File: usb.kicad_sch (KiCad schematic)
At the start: 15 parts, among them J1 USB_A, J2 USB_A, J4 USB_C_Receptacle_USB2.0, U1 FE1.1s, U3 SRV05-4, U4 SRV05-4, Y1 12MHz

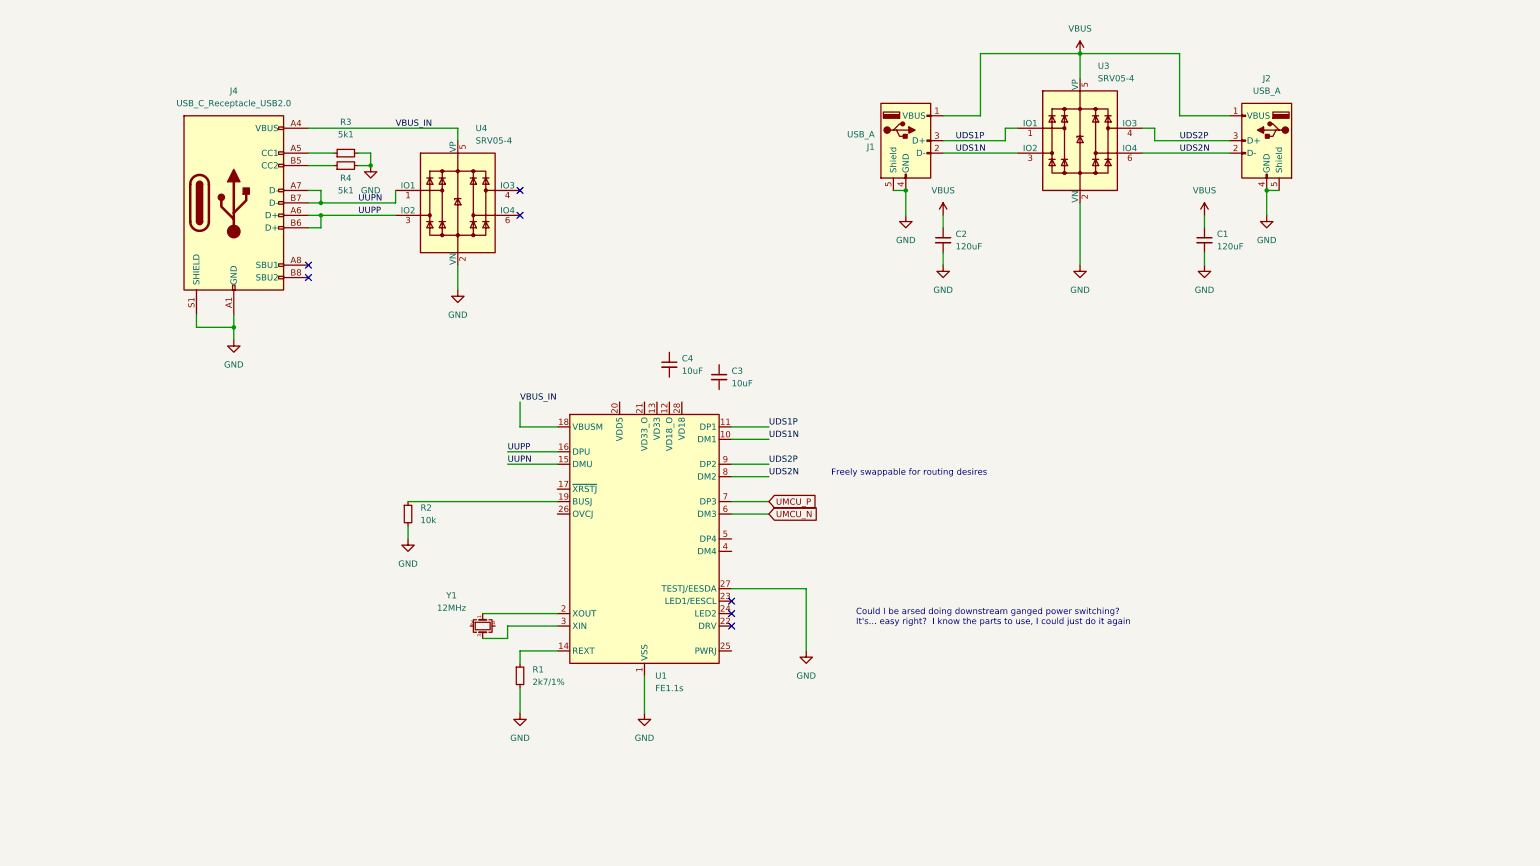
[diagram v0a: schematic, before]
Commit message: sch nearing completion.
usb side done.
needs mcu power supply sorting out.
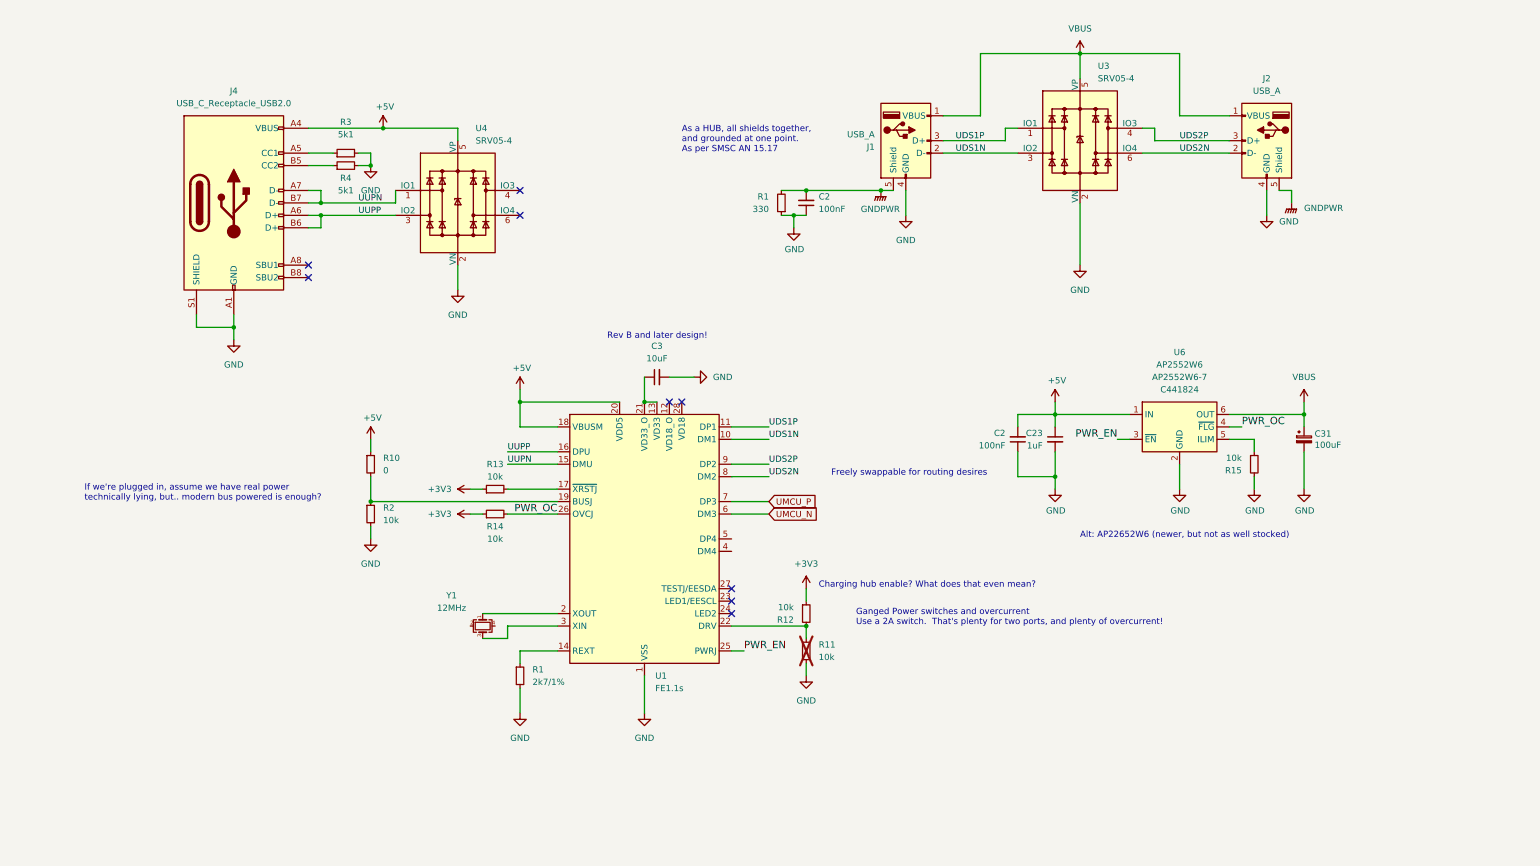
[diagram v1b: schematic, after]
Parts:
- removed C1, C2: 120uF, Capacitor_SMD:C_1206_3216Metric, symbol Device:C_Small
- removed C4: 10uF, Capacitor_SMD:C_0805_2012Metric, symbol Device:C_Small
- added C2 (x2): 100nF, Capacitor_SMD:C_0603_1608Metric, symbol Device:C_Small
- added C23: 1uF, Capacitor_SMD:C_0603_1608Metric, symbol Device:C_Small
- added C31: 100uF, Capacitor_SMD:C_1206_3216Metric, symbol Device:C_Polarized_Small
- added R1: 330, Resistor_SMD:R_0603_1608Metric, symbol Device:R_Small
- added R10: 0, Resistor_SMD:R_0603_1608Metric, symbol Device:R_Small
- added R11, R12, R13, R14, R15: 10k, Resistor_SMD:R_0603_1608Metric, symbol Device:R_Small
- added U6: AP2552W6, Package_TO_SOT_SMD:SOT-23-6, symbol karl-parts:AP2552W6
- C3: MPN (none) -> CL21A106KAYNNNE; jlc-basic (none) -> 1; lcsc# (none) -> C15850
- R1: MPN (none) -> 0603WAF2701T5E; jlc-basic (none) -> 1; lcsc# (none) -> C13167
- R2: MPN (none) -> 0603WAF1002T5E; jlc-basic (none) -> 1; lcsc# (none) -> C25804
- R3, R4: MPN (none) -> 0603WAF5101T5E; jlc-basic (none) -> 1; lcsc# (none) -> C23186
- U1: jlc-basic (none) -> 0
- U3, U4: jlc-basic (none) -> 1; lcsc# C5180248 -> C85364
- Y1: jlc-basic (none) -> 1
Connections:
- net VBUS_IN is gone; now on net +5V: J4.A4 (VBUS), J4.A9 (VBUS), J4.B4 (VBUS), J4.B9 (VBUS), U1.18 (VBUSM), U4.5 (VP)
- net GND: now also C3.2, C2.1, C2.1, C23.2, C31.2, R1.1, R11.1, R15.2, U6.2 (GND); no longer J1.5 (Shield), J2.5 (Shield), U1.27 (TESTJ/EESDA)
- net VBUS: now also C31.1, U6.6 (OUT)
- net at R2.1, U1.19 (BUSJ): now also R10.2
- net at C3.1: now also U1.13 (VD33), U1.21 (VD33_O)
- net at U1.17 (~{XRSTJ}): now also R13.2
- net +5V: now reaches U1.20 (VDD5)
- net +5V: now also C2.2, C23.1, R10.1, U6.1 (IN)
- net at U1.22 (DRV): now also R11.2, R12.2
- net PWR_EN: now reaches U1.25 (PWRJ)
- net PWR_EN: now also U6.3 (~{EN})
- net PWR_OC: now reaches U1.26 (OVCJ)
- net PWR_OC: now also R14.2, U6.4 (~{FLG})
- new net: R15.1, U6.5 (ILIM)
- new net +3V3: R12.1, R13.1, R14.1
- new net GNDPWR: C2.2, J1.5 (Shield), J2.5 (Shield), R1.2
- no-connect marks 7 -> 9
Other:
- note added: "Alt: AP22652W6 (newer, but not as well stocked)"
- note added: "As a HUB, all shields together, and grounded at one point. As per SMSC AN 15.17"
- note added: "Charging hub enable? What does that even mean?"
- note added: "Ganged Power switches and overcurrent Use a 2A switch. That's plenty for two ports, and plenty of overcurrent!"
- note added: "If we're plugged in, assume we have real power technically lying, but.. modern bus powered is enough?"
- note added: "Rev B and later design!"
- note removed: "Could I be arsed doing downstream ganged power switching? It's... easy right? I know the parts to use, I could just do it again"
- moved on the sheet: C3, R2

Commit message: schematic "done" footprints all assigned
Need working calipers to start getting the board outline and fixed
positions, but ... mostly there?

schematic needs "polish" now, more introductions, cleaner text layouts,
probably more optional test points, throw more caps at it.
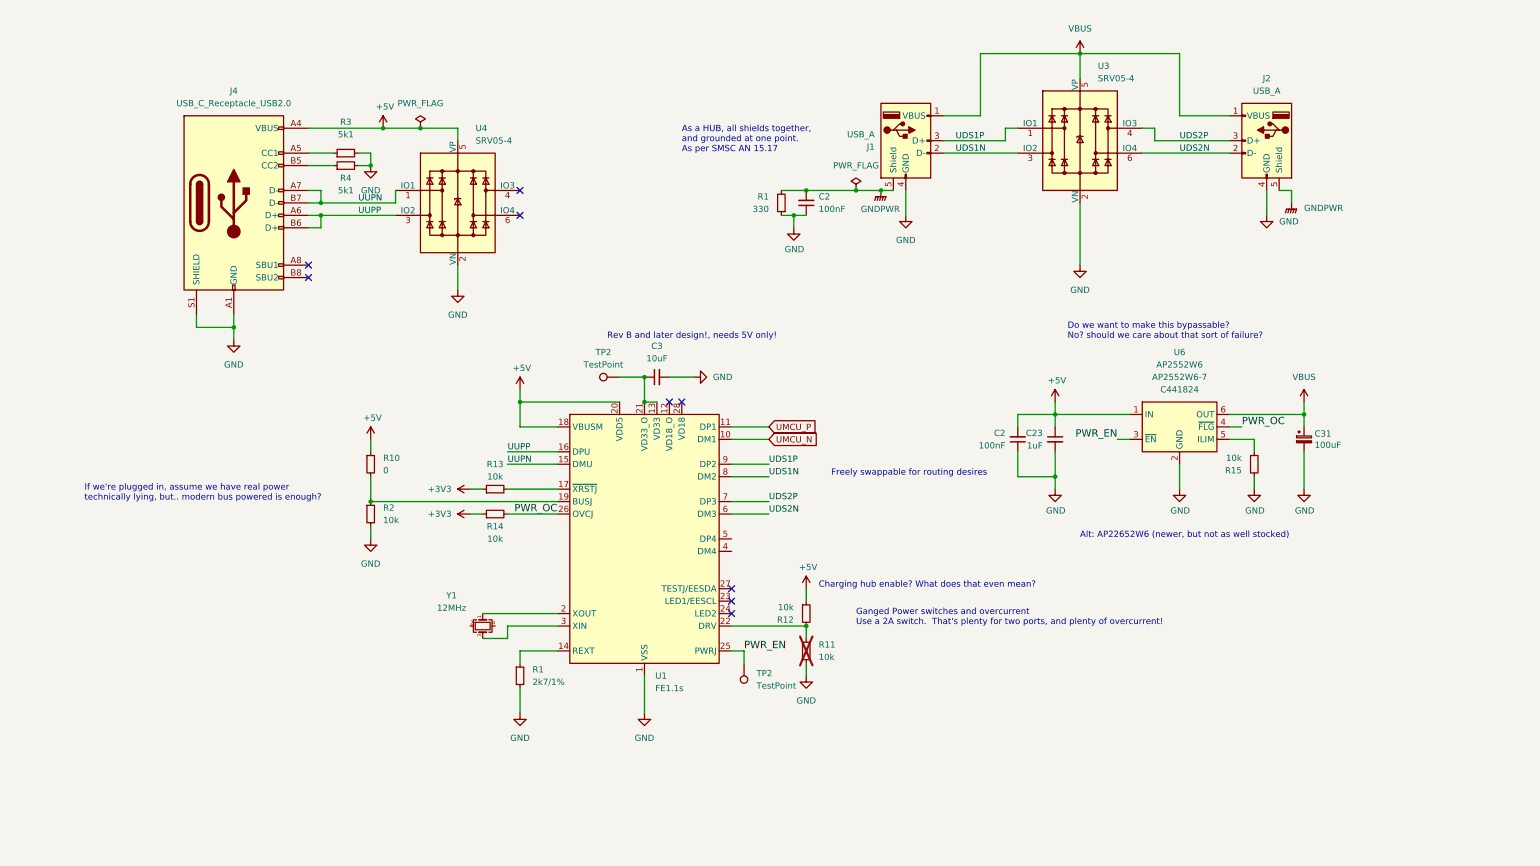
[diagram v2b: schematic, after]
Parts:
- added TP2 (x2): TestPoint, TestPoint:TestPoint_THTPad_D1.5mm_Drill0.7mm, symbol Connector:TestPoint
- J1, J2: footprint (none) -> Connector_USB:USB_A_Stewart_SS-52100-001_Horizontal; MPN (none) -> 902-141A1011D10100; jlc-basic (none) -> 0; lcsc# C42436 -> C42643
- J4: footprint (none) -> Connector_USB:USB_C_Receptacle_G-Switch_GT-USB-7010ASV; MPN (none) -> USB-TYPE-C-018; jlc-basic (none) -> 0; lcsc# C2765186 -> C2927038
- R1, R3, R4: footprint (none) -> Resistor_SMD:R_0603_1608Metric
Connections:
- net +3V3: no longer R12.1
- net +5V: now also R12.1
- net PWR_EN: now also TP2.1
- net UDS1N: now also U1.8 (DM2); no longer U1.10 (DM1)
- net UDS1P: now also U1.9 (DP2); no longer U1.11 (DP1)
- net UDS2N: now also U1.6 (DM3); no longer U1.8 (DM2)
- net UDS2P: now also U1.7 (DP3); no longer U1.9 (DP2)
- net UMCU_N: now also U1.10 (DM1); no longer U1.6 (DM3)
- net UMCU_P: now also U1.11 (DP1); no longer U1.7 (DP3)
- net at C3.1, U1.13 (VD33), U1.21 (VD33_O): now also TP2.1
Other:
- note added: "Do we want to make this bypassable? No? should we care about that sort of failure?"
- note added: "Rev B and later design!, needs 5V only!"
- note removed: "Rev B and later design!"

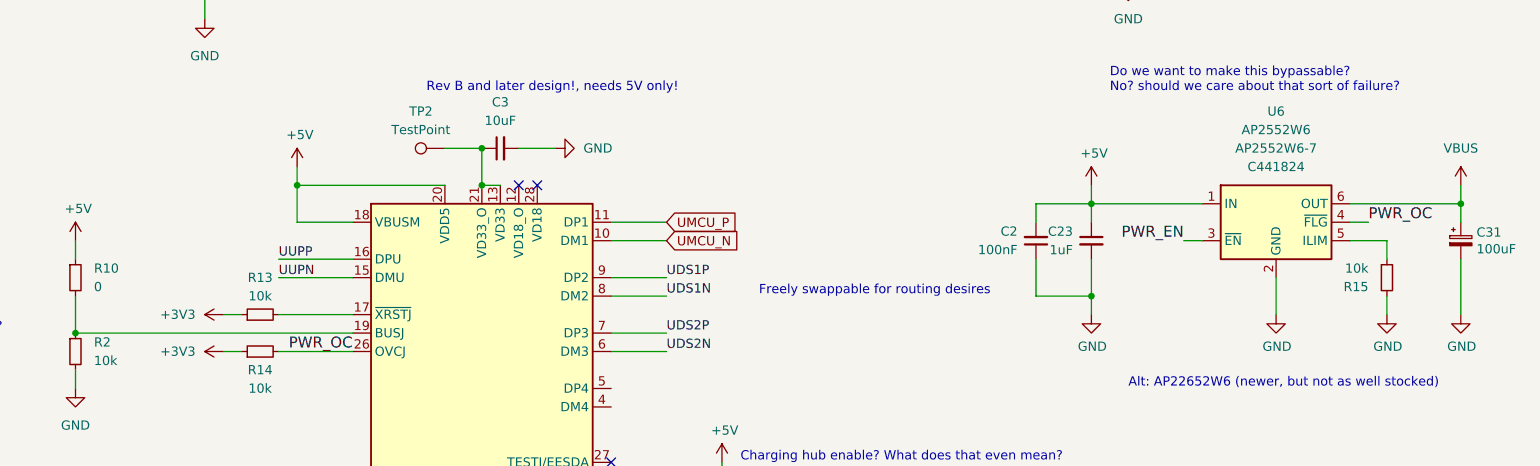
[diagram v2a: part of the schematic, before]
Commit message: import board outline and lock fixed items
No routing, just rough placement of all the fixed items.
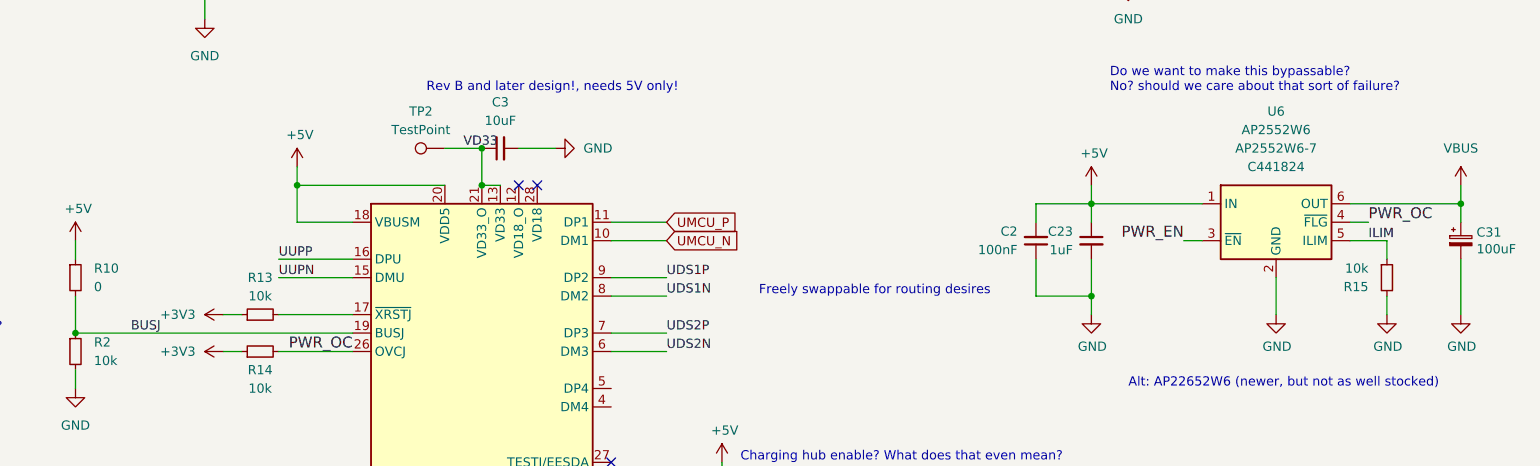
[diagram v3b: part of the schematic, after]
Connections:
- net ILIM: now reaches R15.1, U6.5 (ILIM)
- net BUSJ: now reaches R10.2, R2.1, U1.19 (BUSJ)
- net VD33: now reaches C3.1, TP2.1, U1.13 (VD33), U1.21 (VD33_O)
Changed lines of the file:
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@@
+    (effects (font (size 1.27 1.27)) (justify left bottom))
+  )
+  (label "BUSJ" (at 93.98 114.3 0) (fields_autoplaced)
     (effects (font (size 1.27 1.27)) (justify left bottom))
   )
@@
     (effects (font (size 1.27 1.27)) (justify left bottom))
   )
+  (label "VD33" (at 139.7 88.9 0) (fields_autoplaced)
+    (effects (font (size 1.27 1.27)) (justify left bottom))
+  )
+  (label "ILIM" (at 264.16 101.6 0) (fields_autoplaced)
+    (effects (font (size 1.27 1.27)) (justify left bottom))
+  )

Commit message: add "bonus" can transceiver ;)
this is so we can use the round 1 protos for another project...

also: replace srv05 with an alternate, also jlc preferred, but cheaper
part.  Update power budgets.

We've done some initial work with the pcb, but we're running into weird
kicad wx bugs, so we're going to save it all here, and commit, and
perhaps continue with 7.99.....
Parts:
- U3, U4: lcsc# C85364 -> C7420376; lcsc2# (none) -> C85364
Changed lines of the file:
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@@
+      (effects (font (size 1.27 1.27)) hide)
+    )
+    (property "lcsc2#" "" (at 170.18 53.34 0)
       (effects (font (size 1.27 1.27)) hide)
     )
@@
       (effects (font (size 1.27 1.27)) hide)
     )
-    (property "lcsc#" "C85364" (at 104.14 53.34 0)
+    (property "lcsc#" "C7420376" (at 104.14 53.34 0)
       (effects (font (size 1.27 1.27)) hide)
     )
     (property "jlc-basic" "1" (at 104.14 53.34 0)
+      (effects (font (size 1.27 1.27)) hide)
+    )
+    (property "lcsc2#" "C85364" (at 104.14 53.34 0)
       (effects (font (size 1.27 1.27)) hide)
     )
@@
     )
     (property "jlc-basic" "0" (at 58.42 53.34 0)
+      (effects (font (size 1.27 1.27)) hide)
+    )
+    (property "lcsc2#" "" (at 58.42 53.34 0)
       (effects (font (size 1.27 1.27)) hide)
     )
@@
       (effects (font (size 1.27 1.27)) hide)
     )
+    (property "lcsc2#" "" (at 269.24 40.64 0)
+      (effects (font (size 1.27 1.27)) hide)
+    )
     (pin "1")
     (pin "2")
@@
       (effects (font (size 1.27 1.27)) hide)
     )
+    (property "lcsc2#" "" (at 116.84 149.86 0)
+      (effects (font (size 1.27 1.27)) hide)
+    )
     (pin "1")
     (pin "2")
@@
       (effects (font (size 1.27 1.27)) hide)
     )
+    (property "lcsc2#" "" (at 266.7 106.68 0)
+      (effects (font (size 1.27 1.27)) hide)
+    )
     (pin "1")
     (pin "2")
@@
     )
     (property "jlc-basic" "1" (at 81.28 43.18 0)
+      (effects (font (size 1.27 1.27)) hide)
+    )
+    (property "lcsc2#" "" (at 81.28 43.18 0)
       (effects (font (size 1.27 1.27)) hide)
     )
@@
       (effects (font (size 1.27 1.27)) hide)
     )
+    (property "lcsc2#" "" (at 86.36 116.84 0)
+      (effects (font (size 1.27 1.27)) hide)
+    )
     (pin "1")
     (pin "2")
@@
     )
     (property "jlc-basic" "1" (at 111.76 111.76 0)
+      (effects (font (size 1.27 1.27)) hide)
+    )
+    (property "lcsc2#" "" (at 111.76 111.76 0)
       (effects (font (size 1.27 1.27)) hide)
     )
@@
       (effects (font (size 1.27 1.27)) hide)
     )
+    (property "lcsc2#" "" (at 137.16 88.9 0)
+      (effects (font (size 1.27 1.27)) hide)
+    )
     (pin "1")
     (instances
@@
     )
     (property "Datasheet" "~" (at 157.48 147.32 0)
+      (effects (font (size 1.27 1.27)) hide)
+    )
+    (property "lcsc2#" "" (at 162.56 147.32 0)
       (effects (font (size 1.27 1.27)) hide)
     )
@@
       (effects (font (size 1.27 1.27)) hide)
     )
+    (property "lcsc2#" "" (at 144.78 88.9 0)
+      (effects (font (size 1.27 1.27)) hide)
+    )
     (pin "1")
     (pin "2")
@@
       (effects (font (size 1.27 1.27)) hide)
     )
+    (property "lcsc2#" "" (at 175.26 53.34 0)
+      (effects (font (size 1.27 1.27)) hide)
+    )
     (pin "1")
     (pin "2")
@@
     )
     (property "jlc-basic" "1" (at 218.44 101.6 0)
+      (effects (font (size 1.27 1.27)) hide)
+    )
+    (property "lcsc2#" "" (at 218.44 101.6 0)
       (effects (font (size 1.27 1.27)) hide)
     )
@@
       (effects (font (size 1.27 1.27)) hide)
     )
+    (property "lcsc2#" "" (at 175.26 144.78 0)
+      (effects (font (size 1.27 1.27)) hide)
+    )
     (pin "1")
     (pin "2")
@@
       (effects (font (size 1.27 1.27)) hide)
     )
+    (property "lcsc2#" "" (at 175.26 137.16 0)
+      (effects (font (size 1.27 1.27)) hide)
+    )
     (pin "1")
     (pin "2")
@@
       (effects (font (size 1.27 1.27)) hide)
     )
-    (property "lcsc#" "C85364" (at 231.14 40.64 0)
+    (property "lcsc#" "C7420376" (at 231.14 40.64 0)
       (effects (font (size 1.27 1.27)) hide)
     )
     (property "jlc-basic" "1" (at 231.14 40.64 0)
+      (effects (font (size 1.27 1.27)) hide)
+    )
+    (property "lcsc2#" "C85364" (at 231.14 40.64 0)
       (effects (font (size 1.27 1.27)) hide)
     )
@@
       (effects (font (size 1.27 1.27)) hide)
     )
+    (property "lcsc2#" "" (at 109.22 139.7 0)
+      (effects (font (size 1.27 1.27)) hide)
+    )
     (pin "1")
     (pin "2")
@@
     )
     (property "jlc-basic" "0" (at 142.24 121.92 0)
+      (effects (font (size 1.27 1.27)) hide)
+    )
+    (property "lcsc2#" "" (at 142.24 121.92 0)
       (effects (font (size 1.27 1.27)) hide)
     )
@@
       (effects (font (size 1.27 1.27)) hide)
     )
+    (property "lcsc2#" "" (at 195.58 40.64 0)
+      (effects (font (size 1.27 1.27)) hide)
+    )
     (pin "1")
     (pin "2")
@@
       (effects (font (size 1.27 1.27)) hide)
     )
+    (property "lcsc2#" "" (at 226.06 101.6 0)
+      (effects (font (size 1.27 1.27)) hide)
+    )
     (pin "1")
     (pin "2")
@@
       (effects (font (size 1.27 1.27)) hide)
     )
+    (property "lcsc2#" "" (at 86.36 106.68 0)
+      (effects (font (size 1.27 1.27)) hide)
+    )
     (pin "1")
     (pin "2")
@@
     )
     (property "jlc-basic" "1" (at 111.76 116.84 0)
+      (effects (font (size 1.27 1.27)) hide)
+    )
+    (property "lcsc2#" "" (at 111.76 116.84 0)
       (effects (font (size 1.27 1.27)) hide)
     )
@@
       (effects (font (size 1.27 1.27)) hide)
     )
+    (property "lcsc2#" "" (at 276.86 101.6 0)
+      (effects (font (size 1.27 1.27)) hide)
+    )
     (pin "1")
     (pin "2")
@@
       (effects (font (size 1.27 1.27)))
     )
+    (property "lcsc2#" "" (at 251.46 99.06 0)
+      (effects (font (size 1.27 1.27)) hide)
+    )
     (pin "2")
     (pin "6")
@@
       (effects (font (size 1.27 1.27)) hide)
     )
+    (property "lcsc2#" "" (at 81.28 45.72 0)
+      (effects (font (size 1.27 1.27)) hide)
+    )
